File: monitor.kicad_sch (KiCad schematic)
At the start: 43 parts, among them J1 A, J2 B, J3 Abuf, J4 Bbuf, J5 Sum, J6 Gnd, U704 OPA2197D, U76 OPA2189DGK, U77 OPA2388DGK, U78 OPA2189DGK

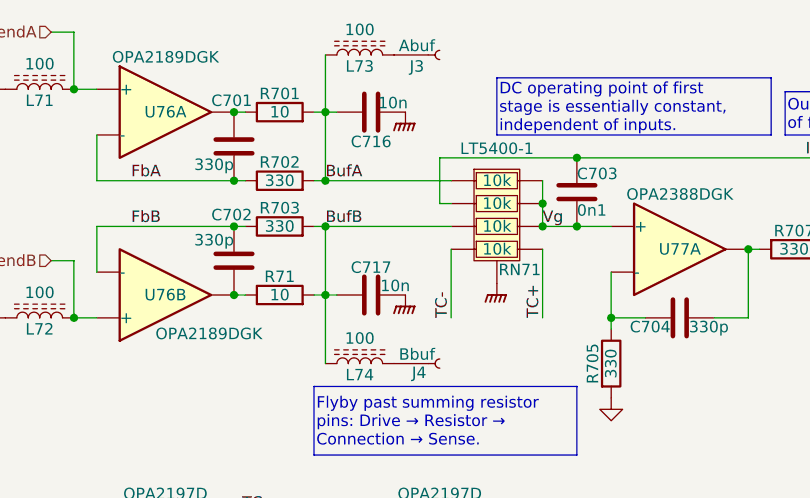
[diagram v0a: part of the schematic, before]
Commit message: Nearly all routed.  Repinning FDA resistors.
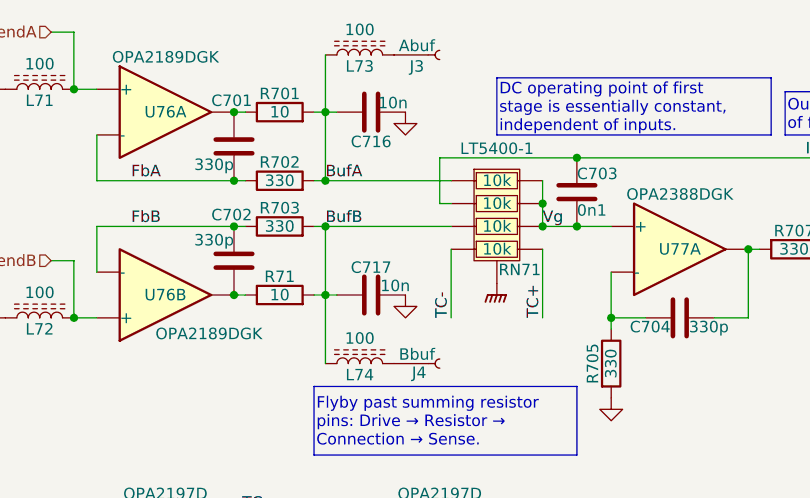
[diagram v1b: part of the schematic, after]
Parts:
- C703: footprint Capacitor_SMD:C_0402_1005Metric -> Capacitor_SMD:C_0603_1608Metric; LCSC C1546 -> (none)
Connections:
- net GND: now also C716.1, C717.1
- net GNDPWR: no longer C716.1, C717.1
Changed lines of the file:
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@@
 	)
 	(symbol
+		(lib_id "power:GND")
+		(at 128.27 72.39 0)
+		(unit 1)
+		(exclude_from_sim no)
+		(in_bom yes)
+		(on_board yes)
+		(dnp no)
+		(property "Reference" "#PWR050"
+			(at 128.27 78.74 0)
+			(effects
+				(font
+					(size 1.27 1.27)
+				)
+				(hide yes)
+			)
+		)
+		(property "Value" "GND"
+			(at 128.27 76.2 0)
+			(effects
+				(font
+					(size 1.27 1.27)
+				)
+				(hide yes)
+			)
+		)
+		(property "Footprint" ""
+			(at 128.27 72.39 0)
+			(effects
+				(font
+					(size 1.27 1.27)
+				)
+				(hide yes)
+			)
+		)
+		(property "Datasheet" ""
+			(at 128.27 72.39 0)
+			(effects
+				(font
+					(size 1.27 1.27)
+				)
+				(hide yes)
+			)
+		)
+		(property "Description" "Power symbol creates a global label with name \"GND\" , ground"
+			(at 128.27 72.39 0)
+			(effects
+				(font
+					(size 1.27 1.27)
+				)
+				(hide yes)
+			)
+		)
+		(pin "1"
+		)
+		(instances
+			(project "lincal"
+				(path "/b054cef4-39e3-49d8-aff0-7ba5a206c187/b0f71c87-958f-452c-ba10-5bfb9905e5da"
+					(reference "#PWR050")
+					(unit 1)
+				)
+			)
+		)
+	)
+	(symbol
 		(lib_id "Parts:OPA2189DGK")
 		(at 209.55 80.01 0)
@@
 	)
 	(symbol
-		(lib_id "power:GNDPWR")
-		(at 128.27 92.71 0)
-		(unit 1)
-		(exclude_from_sim no)
-		(in_bom yes)
-		(on_board yes)
-		(dnp no)
-		(property "Reference" "#PWR0243"
-			(at 128.27 99.06 0)
-			(effects
-				(font
-					(size 1.27 1.27)
-				)
-				(hide yes)
-			)
-		)
-		(property "Value" "GNDPWR"
-			(at 128.27 96.012 0)
-			(effects
-				(font
-					(size 1.27 1.27)
-				)
-				(hide yes)
-			)
-		)
-		(property "Footprint" ""
-			(at 128.27 93.98 0)
-			(effects
-				(font
-					(size 1.27 1.27)
-				)
-				(hide yes)
-			)
-		)
-		(property "Datasheet" ""
-			(at 128.27 93.98 0)
-			(effects
-				(font
-					(size 1.27 1.27)
-				)
-				(hide yes)
-			)
-		)
-		(property "Description" "Power symbol creates a global label with name \"GNDPWR\" , global ground"
-			(at 128.27 92.71 0)
-			(effects
-				(font
-					(size 1.27 1.27)
-				)
-				(hide yes)
-			)
-		)
-		(pin "1"
-		)
-		(instances
-			(project "lincal"
-				(path "/b054cef4-39e3-49d8-aff0-7ba5a206c187/b0f71c87-958f-452c-ba10-5bfb9905e5da"
-					(reference "#PWR0243")
-					(unit 1)
-				)
-			)
-		)
-	)
-	(symbol
 		(lib_id "Device:C")
 		(at 124.46 92.71 270)
@@
 	)
 	(symbol
+		(lib_id "power:GND")
+		(at 128.27 92.71 0)
+		(unit 1)
+		(exclude_from_sim no)
+		(in_bom yes)
+		(on_board yes)
+		(dnp no)
+		(property "Reference" "#PWR045"
+			(at 128.27 99.06 0)
+			(effects
+				(font
+					(size 1.27 1.27)
+				)
+				(hide yes)
+			)
+		)
+		(property "Value" "GND"
+			(at 128.27 96.52 0)
+			(effects
+				(font
+					(size 1.27 1.27)
+				)
+				(hide yes)
+			)
+		)
+		(property "Footprint" ""
+			(at 128.27 92.71 0)
+			(effects
+				(font
+					(size 1.27 1.27)
+				)
+				(hide yes)
+			)
+		)
+		(property "Datasheet" ""
+			(at 128.27 92.71 0)
+			(effects
+				(font
+					(size 1.27 1.27)
+				)
+				(hide yes)
+			)
+		)
+		(property "Description" "Power symbol creates a global label with name \"GND\" , ground"
+			(at 128.27 92.71 0)
+			(effects
+				(font
+					(size 1.27 1.27)
+				)
+				(hide yes)
+			)
+		)
+		(pin "1"
+		)
+		(instances
+			(project "lincal"
+				(path "/b054cef4-39e3-49d8-aff0-7ba5a206c187/b0f71c87-958f-452c-ba10-5bfb9905e5da"
+					(reference "#PWR045")
+					(unit 1)
+				)
+			)
+		)
+	)
+	(symbol
 		(lib_id "Device:C")
 		(at 158.75 95.25 270)
@@
 			)
 		)
-		(property "Footprint" "Capacitor_SMD:C_0402_1005Metric"
+		(property "Footprint" "Capacitor_SMD:C_0603_1608Metric"
 			(at 148.2852 85.09 0)
 			(effects
@@
 			)
 		)
-		(property "LCSC" "C1546"
+		(property "LCSC" ""
 			(at 147.32 81.28 0)
 			(effects
@@
 					(unit 1)
 				)
-			)
-		)
-	)
-	(symbol
-		(lib_id "power:GNDPWR")
-		(at 128.27 72.39 0)
-		(unit 1)
-		(exclude_from_sim no)
-		(in_bom yes)
-		(on_board yes)
-		(dnp no)
-		(property "Reference" "#PWR0242"
-			(at 128.27 78.74 0)
-			(effects
-				(font
-					(size 1.27 1.27)
-				)
-				(hide yes)
-			)
-		)
-		(property "Value" "GNDPWR"
-			(at 128.27 75.692 0)
-			(effects
-				(font
-					(size 1.27 1.27)
-				)
-				(hide yes)
-			)
-		)
-		(property "Footprint" ""
-			(at 128.27 73.66 0)
-			(effects
-				(font
-					(size 1.27 1.27)
-				)
-				(hide yes)
-			)
-		)
-		(property "Datasheet" ""
-			(at 128.27 73.66 0)
-			(effects
-				(font
-					(size 1.27 1.27)
-				)
-				(hide yes)
-			)
-		)
-		(property "Description" "Power symbol creates a global label with name \"GNDPWR\" , global ground"
-			(at 128.27 72.39 0)
-			(effects
-				(font
-					(size 1.27 1.27)
-				)
-				(hide yes)
-			)
-		)
-		(pin "1"
-		)
-		(instances
-			(project "lincal"
-				(path "/b054cef4-39e3-49d8-aff0-7ba5a206c187/b0f71c87-958f-452c-ba10-5bfb9905e5da"
-					(reference "#PWR0242")
-					(unit 1)
-				)

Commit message: Put in some IO resistors.
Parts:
- R704: renamed from L71; footprint Inductor_SMD:L_0603_1608Metric -> Resistor_SMD:R_0402_1005Metric; symbol Device:L_Ferrite -> Device:R; LCSC C14709 -> C25076
- R706: renamed from L72; footprint Inductor_SMD:L_0603_1608Metric -> Resistor_SMD:R_0402_1005Metric; symbol Device:L_Ferrite -> Device:R; LCSC C14709 -> C25076
- R714: renamed from L73; footprint Inductor_SMD:L_0603_1608Metric -> Resistor_SMD:R_0402_1005Metric; symbol Device:L_Ferrite -> Device:R; LCSC C14709 -> C25076
- R715: renamed from L74; footprint Inductor_SMD:L_0603_1608Metric -> Resistor_SMD:R_0402_1005Metric; symbol Device:L_Ferrite -> Device:R; LCSC C14709 -> C25076
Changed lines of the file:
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@@
 	)
 	(symbol
-		(lib_id "Device:L_Ferrite")
+		(lib_id "Device:R")
 		(at 87.63 69.85 90)
 		(unit 1)
@@
 		(on_board yes)
 		(dnp no)
-		(property "Reference" "L71"
-			(at 87.63 71.12 90)
+		(property "Reference" "R704"
+			(at 87.63 67.818 90)
 			(effects
 				(font
@@
 		)
 		(property "Value" "100"
-			(at 87.63 67.056 90)
-			(effects
-				(font
-					(size 1.27 1.27)
-				)
-			)
-		)
-		(property "Footprint" "Inductor_SMD:L_0603_1608Metric"
+			(at 87.63 69.85 90)
+			(effects
+				(font
+					(size 1.27 1.27)
+				)
+			)
+		)
+		(property "Footprint" "Resistor_SMD:R_0402_1005Metric"
+			(at 87.63 71.628 90)
+			(effects
+				(font
+					(size 1.27 1.27)
+				)
+				(hide yes)
+			)
+		)
+		(property "Datasheet" "~"
 			(at 87.63 69.85 0)
 			(effects
@@
 			)
 		)
-		(property "Datasheet" "2A / 50mΩ"
+		(property "Description" "Resistor"
 			(at 87.63 69.85 0)
 			(effects
@@
 			)
 		)
-		(property "Description" "Inductor with ferrite core"
-			(at 87.63 69.85 0)
-			(effects
-				(font
-					(size 1.27 1.27)
-				)
-				(hide yes)
-			)
-		)
-		(property "LCSC" "C14709"
+		(property "LCSC" "C25076"
 			(at 87.63 69.85 90)
 			(effects
@@
 			(project "lincal"
 				(path "/b054cef4-39e3-49d8-aff0-7ba5a206c187/b0f71c87-958f-452c-ba10-5bfb9905e5da"
-					(reference "L71")
+					(reference "R704")
 					(unit 1)
 				)
@@
 	)
 	(symbol
-		(lib_id "Device:L_Ferrite")
+		(lib_id "Device:R")
 		(at 123.19 100.33 90)
 		(unit 1)
@@
 		(on_board yes)
 		(dnp no)
-		(property "Reference" "L74"
-			(at 123.19 101.6 90)
+		(property "Reference" "R715"
+			(at 123.19 98.298 90)
 			(effects
 				(font
@@
 		)
 		(property "Value" "100"
-			(at 123.19 97.536 90)
-			(effects
-				(font
-					(size 1.27 1.27)
-				)
-			)
-		)
-		(property "Footprint" "Inductor_SMD:L_0603_1608Metric"
+			(at 123.19 100.33 90)
+			(effects
+				(font
+					(size 1.27 1.27)
+				)
+			)
+		)
+		(property "Footprint" "Resistor_SMD:R_0402_1005Metric"
+			(at 123.19 102.108 90)
+			(effects
+				(font
+					(size 1.27 1.27)
+				)
+				(hide yes)
+			)
+		)
+		(property "Datasheet" "~"
 			(at 123.19 100.33 0)
 			(effects
@@
 			)
 		)
-		(property "Datasheet" "2A / 50mΩ"
+		(property "Description" "Resistor"
 			(at 123.19 100.33 0)
 			(effects
@@
 			)
 		)
-		(property "Description" "Inductor with ferrite core"
-			(at 123.19 100.33 0)
-			(effects
-				(font
-					(size 1.27 1.27)
-				)
-				(hide yes)
-			)
-		)
-		(property "LCSC" "C14709"
+		(property "LCSC" "C25076"
 			(at 123.19 100.33 90)
 			(effects
@@
 			(project "lincal"
 				(path "/b054cef4-39e3-49d8-aff0-7ba5a206c187/b0f71c87-958f-452c-ba10-5bfb9905e5da"
-					(reference "L74")
+					(reference "R715")
 					(unit 1)
 				)
@@
 	)
 	(symbol
-		(lib_id "Device:L_Ferrite")
+		(lib_id "Device:R")
 		(at 123.19 66.04 90)
 		(unit 1)
@@
 		(on_board yes)
 		(dnp no)
-		(property "Reference" "L73"
-			(at 123.19 67.31 90)
+		(property "Reference" "R714"
+			(at 123.19 64.008 90)
 			(effects
 				(font
@@
 		)
 		(property "Value" "100"
-			(at 123.19 63.246 90)
-			(effects
-				(font
-					(size 1.27 1.27)
-				)
-			)
-		)
-		(property "Footprint" "Inductor_SMD:L_0603_1608Metric"
+			(at 123.19 66.04 90)
+			(effects
+				(font
+					(size 1.27 1.27)
+				)
+			)
+		)
+		(property "Footprint" "Resistor_SMD:R_0402_1005Metric"
+			(at 123.19 67.818 90)
+			(effects
+				(font
+					(size 1.27 1.27)
+				)
+				(hide yes)
+			)
+		)
+		(property "Datasheet" "~"
 			(at 123.19 66.04 0)
 			(effects
@@
 			)
 		)
-		(property "Datasheet" "2A / 50mΩ"
+		(property "Description" "Resistor"
 			(at 123.19 66.04 0)
 			(effects
@@
 			)
 		)
-		(property "Description" "Inductor with ferrite core"
-			(at 123.19 66.04 0)
-			(effects
-				(font
-					(size 1.27 1.27)
-				)
-				(hide yes)
-			)
-		)
-		(property "LCSC" "C14709"
+		(property "LCSC" "C25076"
 			(at 123.19 66.04 90)
 			(effects
@@
 			(project "lincal"
 				(path "/b054cef4-39e3-49d8-aff0-7ba5a206c187/b0f71c87-958f-452c-ba10-5bfb9905e5da"
-					(reference "L73")
+					(reference "R714")
 					(unit 1)
 				)
@@
 	)
 	(symbol
-		(lib_id "Device:L_Ferrite")
+		(lib_id "Device:R")
 		(at 87.63 95.25 90)
 		(unit 1)
@@
 		(on_board yes)
 		(dnp no)
-		(property "Reference" "L72"
-			(at 87.63 96.52 90)
+		(property "Reference" "R706"
+			(at 87.63 93.218 90)
 			(effects
 				(font
@@
 		)
 		(property "Value" "100"
-			(at 87.63 92.456 90)
-			(effects
-				(font
-					(size 1.27 1.27)
-				)
-			)
-		)
-		(property "Footprint" "Inductor_SMD:L_0603_1608Metric"
+			(at 87.63 95.25 90)
+			(effects
+				(font
+					(size 1.27 1.27)
+				)
+			)
+		)
+		(property "Footprint" "Resistor_SMD:R_0402_1005Metric"
+			(at 87.63 97.028 90)
+			(effects
+				(font
+					(size 1.27 1.27)
+				)
+				(hide yes)
+			)
+		)
+		(property "Datasheet" "~"
 			(at 87.63 95.25 0)
 			(effects
@@
 			)
 		)
-		(property "Datasheet" "2A / 50mΩ"
+		(property "Description" "Resistor"
 			(at 87.63 95.25 0)
 			(effects
@@
 			)
 		)
-		(property "Description" "Inductor with ferrite core"
-			(at 87.63 95.25 0)
-			(effects
-				(font
-					(size 1.27 1.27)
-				)
-				(hide yes)
-			)
-		)
-		(property "LCSC" "C14709"
+		(property "LCSC" "C25076"
 			(at 87.63 95.25 90)
 			(effects
@@
 			(project "lincal"
 				(path "/b054cef4-39e3-49d8-aff0-7ba5a206c187/b0f71c87-958f-452c-ba10-5bfb9905e5da"
-					(reference "L72")
-					(unit 1)
-				)
+					(reference "R706")
+					(unit 1)
+				)

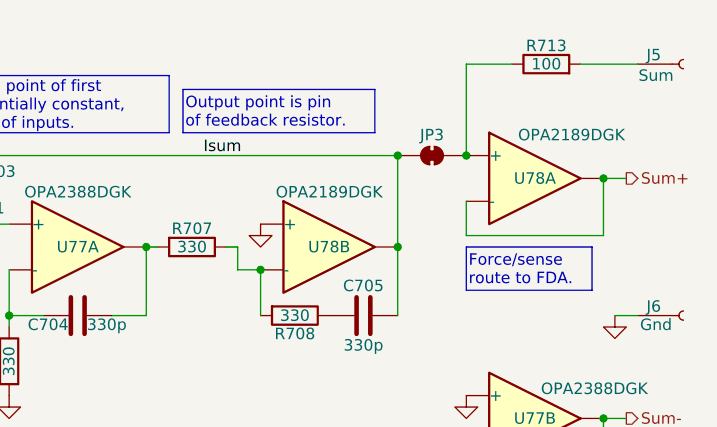
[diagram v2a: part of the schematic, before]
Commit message: DRC update.  Repin ADC.  De-crack the S/H ground.
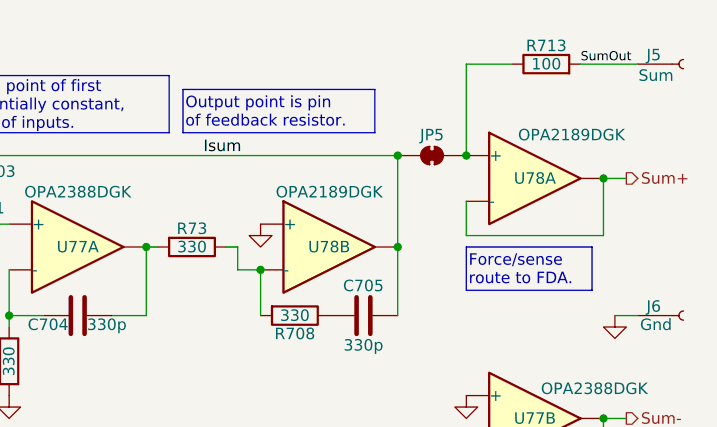
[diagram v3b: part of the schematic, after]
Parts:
- renumbered JP3 to JP5, R707 to R73
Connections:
- net SumOut: now reaches J5.1 (Pin_1), R713.2
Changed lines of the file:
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@@
 		)
 	)
+	(label "SumOut"
+		(at 214.63 67.31 0)
+		(effects
+			(font
+				(size 1.016 1.016)
+			)
+			(justify left bottom)
+		)
+	)
 	(label "BufB"
 		(at 119.38 85.09 0)
@@
 		(on_board yes)
 		(dnp no)
-		(property "Reference" "R707"
+		(property "Reference" "R73"
 			(at 171.45 85.598 90)
 			(effects
@@
 			(project "lincal"
 				(path "/b054cef4-39e3-49d8-aff0-7ba5a206c187/b0f71c87-958f-452c-ba10-5bfb9905e5da"
-					(reference "R707")
+					(reference "R73")
 					(unit 1)
 				)
@@
 		(on_board yes)
 		(dnp no)
-		(property "Reference" "JP3"
+		(property "Reference" "JP5"
 			(at 198.12 75.184 0)
 			(effects
@@
 			(project ""
 				(path "/b054cef4-39e3-49d8-aff0-7ba5a206c187/b0f71c87-958f-452c-ba10-5bfb9905e5da"
-					(reference "JP3")
+					(reference "JP5")
 					(unit 1)
 				)

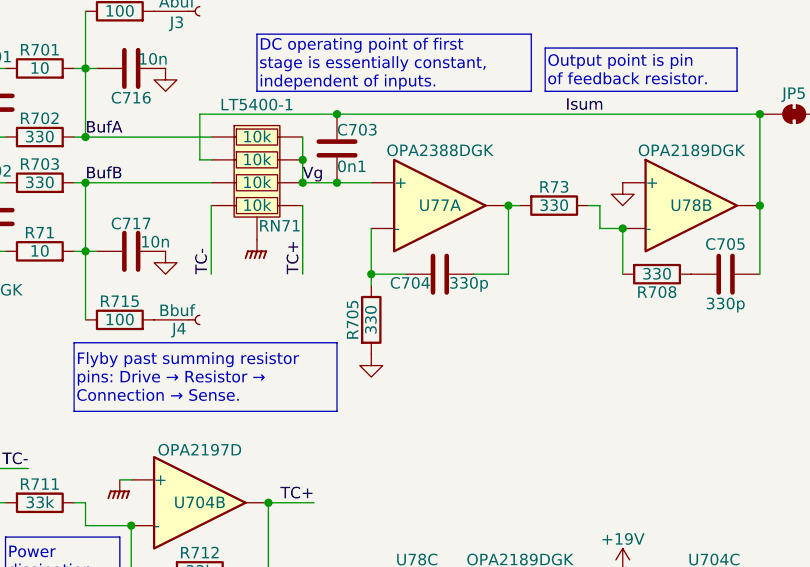
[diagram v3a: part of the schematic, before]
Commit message: Redo the SPI routing to DAC.
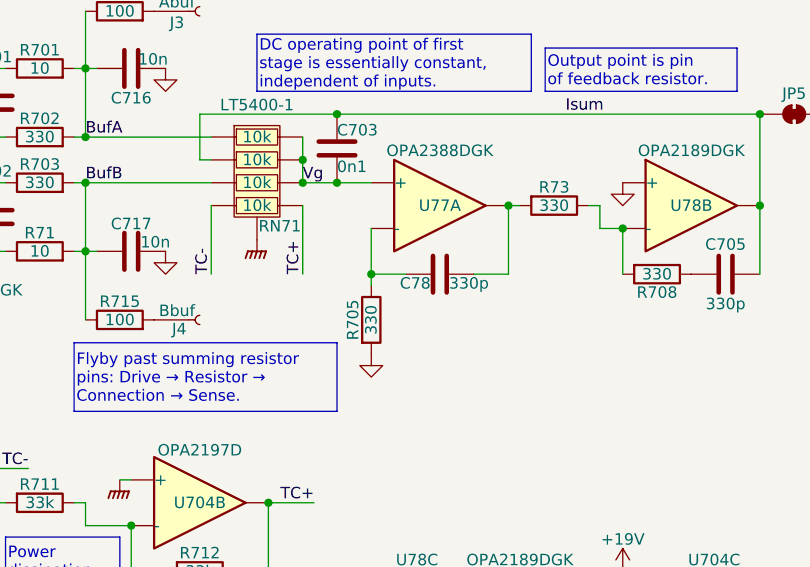
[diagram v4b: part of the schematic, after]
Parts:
- renumbered C704 to C78
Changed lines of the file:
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@@
 		(on_board yes)
 		(dnp no)
-		(property "Reference" "C704"
+		(property "Reference" "C78"
 			(at 157.734 96.266 90)
 			(effects
@@
 			(project "lincal"
 				(path "/b054cef4-39e3-49d8-aff0-7ba5a206c187/b0f71c87-958f-452c-ba10-5bfb9905e5da"
-					(reference "C704")
+					(reference "C78")
 					(unit 1)
 				)

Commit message: More component metadata.
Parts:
- C701, C702, C705, C710, C711, C712, C713, C714, C715, C716, C717, C718, C719, C78, R701, R702, R703, R704, R705, R706, R708, R709, R71, R710, R711, R712, R713, R714, R715, R73, RN71: Stock (none) -> JLC
- C703: LCSC (none) -> C14858; Stock (none) -> JLC
- J1, J2, J3, J4, J5, J6, JP5: Stock (none) -> Board
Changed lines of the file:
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@@
 			)
 		)
-		(property "Stock" ""
+		(property "Stock" "JLC"
 			(at 114.3 92.71 90)
 			(effects
@@
 			)
 		)
-		(property "Stock" ""
+		(property "Stock" "JLC"
 			(at 109.22 76.2 0)
 			(effects
@@
 			)
 		)
-		(property "Stock" ""
+		(property "Stock" "JLC"
 			(at 124.46 92.71 90)
 			(effects
@@
 			)
 		)
-		(property "Stock" ""
+		(property "Stock" "Board"
 			(at 132.08 100.33 0)
 			(effects
@@
 			)
 		)
-		(property "Stock" ""
+		(property "Stock" "JLC"
 			(at 158.75 95.25 90)
 			(effects
@@
 			)
 		)
-		(property "Stock" ""
+		(property "Stock" "Board"
 			(at 132.08 66.04 0)
 			(effects
@@
 			)
 		)
-		(property "Stock" ""
+		(property "Stock" "JLC"
 			(at 185.42 132.08 0)
 			(effects
@@
 			)
 		)
-		(property "Stock" ""
+		(property "Stock" "JLC"
 			(at 213.36 139.7 0)
 			(effects
@@
 			)
 		)
-		(property "Stock" ""
+		(property "Stock" "JLC"
 			(at 210.82 67.31 90)
 			(effects
@@
 			)
 		)
-		(property "Stock" ""
+		(property "Stock" "JLC"
 			(at 138.43 85.09 0)
 			(effects
@@
 			)
 		)
-		(property "Stock" ""
+		(property "Stock" "Board"
 			(at 226.06 95.25 0)
 			(effects
@@
 			)
 		)
-		(property "Stock" ""
+		(property "Stock" "JLC"
 			(at 87.63 69.85 90)
 			(effects
@@
 			)
 		)
-		(property "Stock" ""
+		(property "Stock" "Board"
 			(at 78.74 95.25 0)
 			(effects
@@
 			)
 		)
-		(property "Stock" ""
+		(property "Stock" "JLC"
 			(at 171.45 87.63 90)
 			(effects
@@
 			)
 		)
-		(property "Stock" ""
+		(property "Stock" "JLC"
 			(at 114.3 120.65 90)
 			(effects
@@
 			)
 		)
-		(property "Stock" ""
+		(property "Stock" "Board"
 			(at 78.74 69.85 0)
 			(effects
@@
 			)
 		)
-		(property "Stock" ""
+		(property "Stock" "JLC"
 			(at 114.3 80.01 90)
 			(effects
@@
 			)
 		)
-		(property "Stock" ""
+		(property "Stock" "JLC"
 			(at 114.3 85.09 90)
 			(effects
@@
 			)
 		)
-		(property "Stock" ""
+		(property "Stock" "JLC"
 			(at 171.45 132.08 0)
 			(effects
@@
 			)
 		)
-		(property "LCSC" ""
+		(property "LCSC" "C14858"
 			(at 147.32 81.28 0)
 			(effects
@@
 			)
 		)
-		(property "Stock" ""
+		(property "Stock" "JLC"
 			(at 147.32 81.28 0)
 			(effects
@@
 			)
 		)
-		(property "Stock" ""
+		(property "Stock" "JLC"
 			(at 114.3 72.39 90)
 			(effects
@@
 			)
 		)
-		(property "Stock" ""
+		(property "Stock" "JLC"
 			(at 101.6 128.27 90)
 			(effects
@@
 			)
 		)
-		(property "Stock" ""
+		(property "Stock" "JLC"
 			(at 123.19 100.33 90)
 			(effects
@@
 			)
 		)
-		(property "Stock" ""
+		(property "Stock" "JLC"
 			(at 123.19 66.04 90)
 			(effects
@@
 			)
 		)
-		(property "Stock" ""
+		(property "Stock" "JLC"
 			(at 87.63 95.25 90)
 			(effects
@@
 			)
 		)
-		(property "Stock" ""
+		(property "Stock" "JLC"
 			(at 109.22 88.9 0)
 			(effects
@@
 			)
 		)
-		(property "Stock" ""
+		(property "Stock" "JLC"
 			(at 185.42 139.7 0)
 			(effects
@@
 			)
 		)
-		(property "Stock" ""
+		(property "Stock" "JLC"
 			(at 151.13 100.33 90)
 			(effects
@@
 			)
 		)
-		(property "Stock" ""
+		(property "Stock" "JLC"
 			(at 190.5 95.25 90)
 			(effects
@@
 			)
 		)
-		(property "Stock" ""
+		(property "Stock" "JLC"
 			(at 160.02 139.7 0)
 			(effects
@@
 			)
 		)
-		(property "Stock" ""
+		(property "Stock" "JLC"
 			(at 171.45 139.7 0)
 			(effects
@@
 			)
 		)
-		(property "Stock" ""
+		(property "Stock" "JLC"
 			(at 88.9 123.19 90)
 			(effects
@@
 			)
 		)
-		(property "Stock" ""
+		(property "Stock" "JLC"
 			(at 132.08 128.27 90)
 			(effects
@@
 			)
 		)
-		(property "Stock" ""
+		(property "Stock" "JLC"
 			(at 124.46 72.39 90)
 			(effects
@@
 			)
 		)
-		(property "Stock" ""
+		(property "Stock" "JLC"
 			(at 213.36 132.08 0)
 			(effects
@@
 			)
 		)
-		(property "Stock" ""
+		(property "Stock" "JLC"
 			(at 160.02 132.08 0)
 			(effects
@@
 			)
 		)
-		(property "Stock" ""
+		(property "Stock" "JLC"
 			(at 182.88 95.25 90)
 			(effects
@@
 			)
 		)
-		(property "Stock" ""
+		(property "Stock" "Board"
 			(at 198.12 77.47 0)
 			(effects
@@
 			)
 		)
-		(property "Stock" ""
+		(property "Stock" "Board"
 			(at 226.06 67.31 0)
 			(effects

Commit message: Front panel
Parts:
- R709: value 16k -> 15k; footprint Resistor_SMD:R_0603_1608Metric -> Resistor_SMD:R_0402_1005Metric; LCSC C22818 -> C25756
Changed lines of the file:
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@@
 			)
 		)
-		(property "Value" "16k"
+		(property "Value" "15k"
 			(at 88.9 123.19 90)
 			(effects
@@
 			)
 		)
-		(property "Footprint" "Resistor_SMD:R_0603_1608Metric"
+		(property "Footprint" "Resistor_SMD:R_0402_1005Metric"
 			(at 88.9 121.412 90)
 			(effects
@@
 			)
 		)
-		(property "LCSC" "C22818"
+		(property "LCSC" "C25756"
 			(at 88.9 123.19 90)
 			(effects
